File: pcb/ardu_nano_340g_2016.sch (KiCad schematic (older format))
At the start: 38 parts, among them J1 USB_B_Mini, J2 Conn_01x15, J3 Conn_01x15, J4 Conn_02x03_Odd_Even, U1 CH340G-JEC, U2 ATMEGA328P-AU, U3 LM1117-5.0, Y1 16MHz, Y2 12Mhz

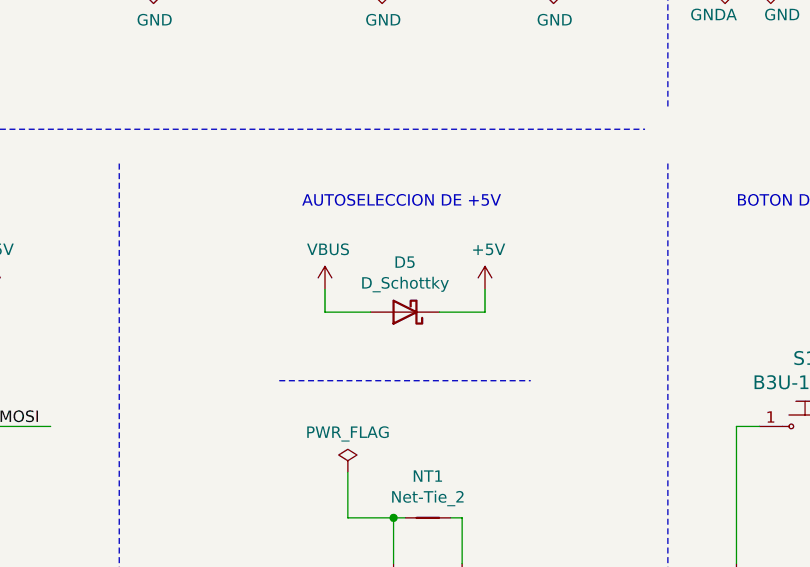
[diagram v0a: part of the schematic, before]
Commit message: versión para fabricación casera con vias grandes
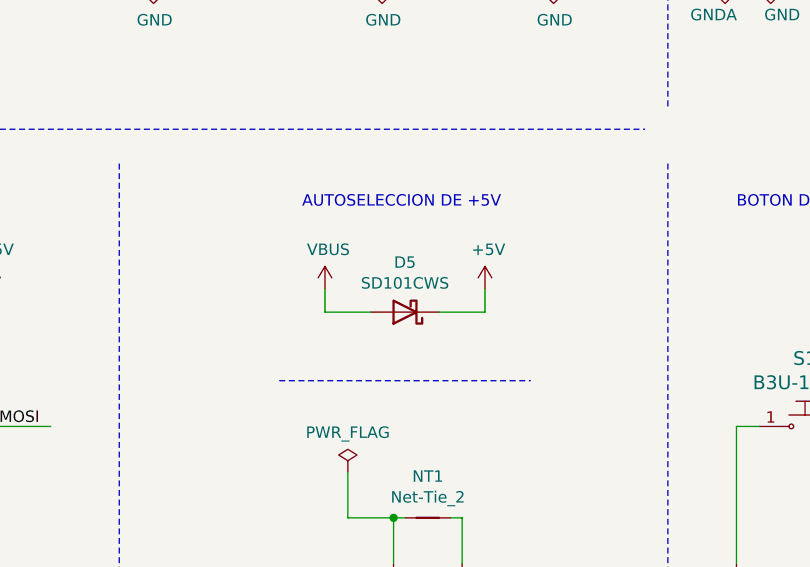
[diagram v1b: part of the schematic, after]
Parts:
- D5: value D_Schottky -> SD101CWS
- J1: footprint Connector_USB:USB_Mini-B_Wuerth_65100516121_Horizontal -> Connector_USB:USB_Mini-B_Lumberg_2486_01_Horizontal
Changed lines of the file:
@@
 Title "ardu_nano_340g_2016"
 Date "2020-10-18"
-Rev "2.3"
+Rev "2.4"
 Comp "Autor: Juan Esteban Carrique <jecarrique@sinc.unl.edu.ar>"
 Comment1 "Revisor par: Alejandro Gorrin"
 Comment2 "Revisor Docente: Diego Brengi"
 Comment3 "Licencia: CC BY-NC-SA"
-Comment4 "V2.3 Se agregó capacitor desacople MCU"
+Comment4 "V2.4 Se agregan vistas 3D y valores faltantes"
 $EndDescr
 $Comp
@@
 F 0 "J1" H 1157 2167 50  0000 C CNN
 F 1 "USB_B_Mini" H 1157 2076 50  0000 C CNN
-F 2 "Connector_USB:USB_Mini-B_Wuerth_65100516121_Horizontal" H 1250 1650 50  0001 C CNN
+F 2 "Connector_USB:USB_Mini-B_Lumberg_2486_01_Horizontal" H 1250 1650 50  0001 C CNN
 F 3 "https://media.digikey.com/pdf/Data%20Sheets/Hirose%20PDFs/UX%20Series.pdf" H 1250 1650 50  0001 C CNN
 F 4 "https://media.digikey.com/pdf/Data%20Sheets/Hirose%20PDFs/UX%20Series.pdf" H 1100 1700 50  0001 C CNN "DK_Datasheet_Link"
@@
 P 3850 5850
 F 0 "D5" H 3850 5633 50  0000 C CNN
-F 1 "D_Schottky" H 3850 5724 50  0000 C CNN
+F 1 "SD101CWS" H 3850 5724 50  0000 C CNN
 F 2 "Diode_SMD:D_SOD-323_HandSoldering" H 3850 5850 50  0001 C CNN
 F 3 "https://www.vishay.com/ppg?85680" H 3850 5850 50  0001 C CNN
